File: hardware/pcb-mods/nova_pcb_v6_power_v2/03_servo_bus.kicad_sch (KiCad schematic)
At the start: 11 parts, among them J3 XT30_Inj, J4 XT30_Inj, J5 XT30_Inj, J6 XT30_Inj, J7 XT30_Inj, J8 ServoBus_TTL

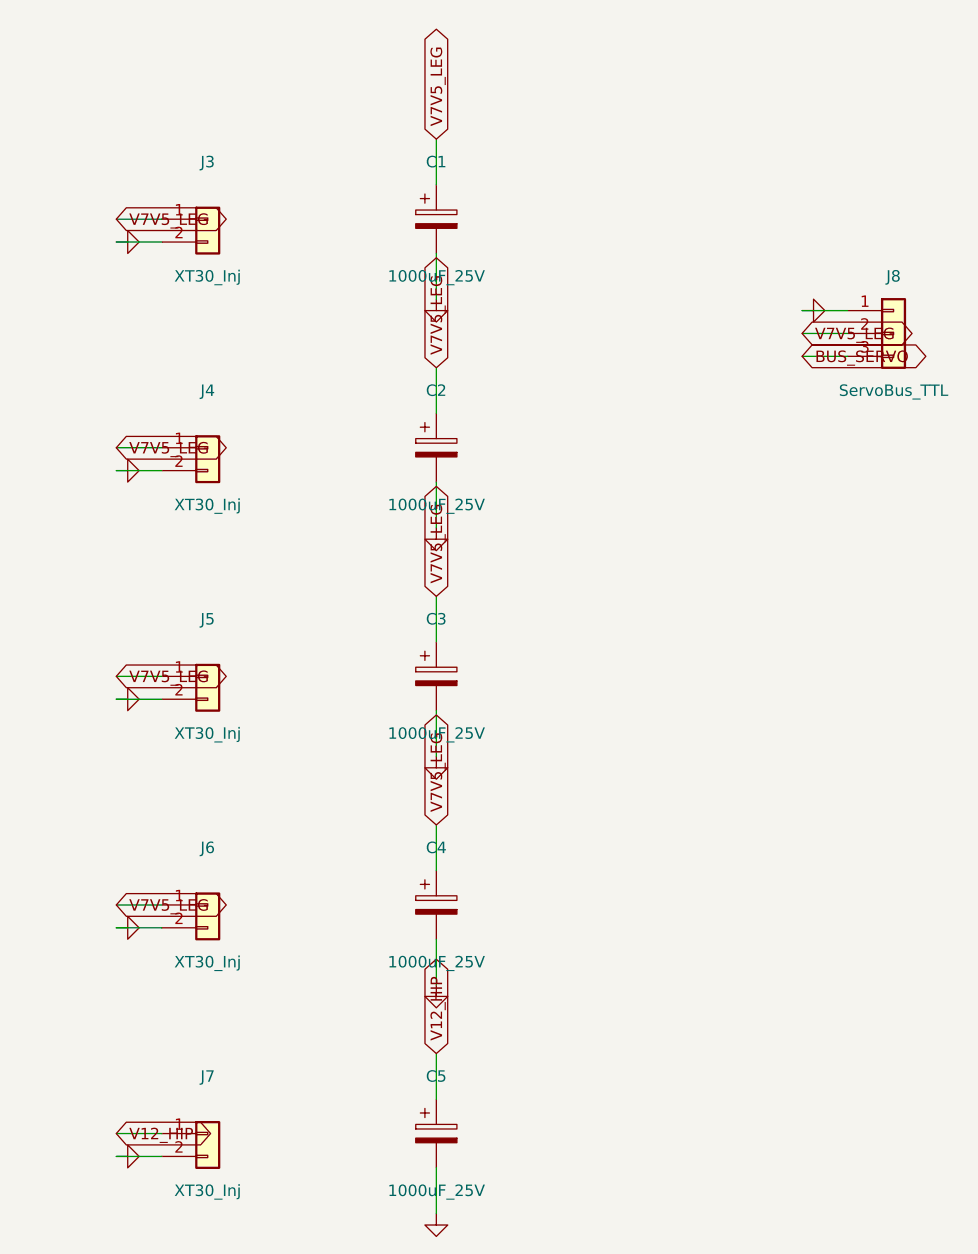
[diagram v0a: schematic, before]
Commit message: Chassis + leg_v6 CAD: no-drill assembly, leg fault audit (LA-1..28 + #47), fastener + gate hardening (#48)
* power board: arm Phase-4 routed + cleaned + fresh gerbers (fab-ready)

Completes the power board (blocker B1):
- U5.EN routed on EN_BUCKS (re-gate now realized on the board).
- V7V5_ARM 3mm, BATT_NEG/VBAT long runs 3mm, 21 high-current pads solid
  zone-connection (current-capacity fixes; TO-220/SW1 escapes left at 1.3mm).
- Removed the duplicate U12 + J14 (F8 UUID-mismatch artifacts) and the full
  orphan dangling-track chain they left behind.
- DRC: 0 hard, 0 unconnected, 0 dangling (10 cosmetic silk/lib only).
- Gerbers regenerated; fab_gate GO on both boards (J20 cross-board match OK).

DNP roster correct (U5 arm buck, U12 arm INA = Phase-4 reserve).

Co-Authored-By: Claude Opus 4.8 <noreply@anthropic.com>

* audit fixes 2026-06-18: NaN guard, pinout/battery/LVC doc sync, STATUS audit block

- main.cpp: NaN guard on commanded position (was UB (uint16_t)NaN -> 0 slam)
- teensy firmware/README.md: pinout table corrected to match main.cpp/PCB v6 (Serial1 0/1, E-stop 5, batt 4, active-LOW OE)
- power-budget.md + BOM.md: battery 4000->6000mAh (real Ovonic packs) + runtime/charge recompute
- BOM.md: bus driver order line -> SN74LVC125A (must be LVC, not 74HC125)
- STATUS.md: cross-domain audit section (open misalignments, weak points, questions)

Co-Authored-By: Claude Opus 4.8 <noreply@anthropic.com>

* docs: add servo-bus half-duplex timing bench checklist (pre-power-on §10)

Co-Authored-By: Claude Opus 4.8 <noreply@anthropic.com>

* docs: battery 4000->6000mAh sweep across secondary docs + STATUS CI-note fix

- 6000mAh 4S Ovonic (real pack) in cad-tooling, notes-qol (SoC math 5400mAh),
  order-list (bag), wiring diagram, README charger note, patterns pocket label
- dimensions.md + patterns.md: physical box/pocket dims flagged RE-MEASURE
  (6000mAh pack is larger; old 4000mAh dims kept as reference, not as truth)
- STATUS.md: corrected CI note (ros-pytest.yml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
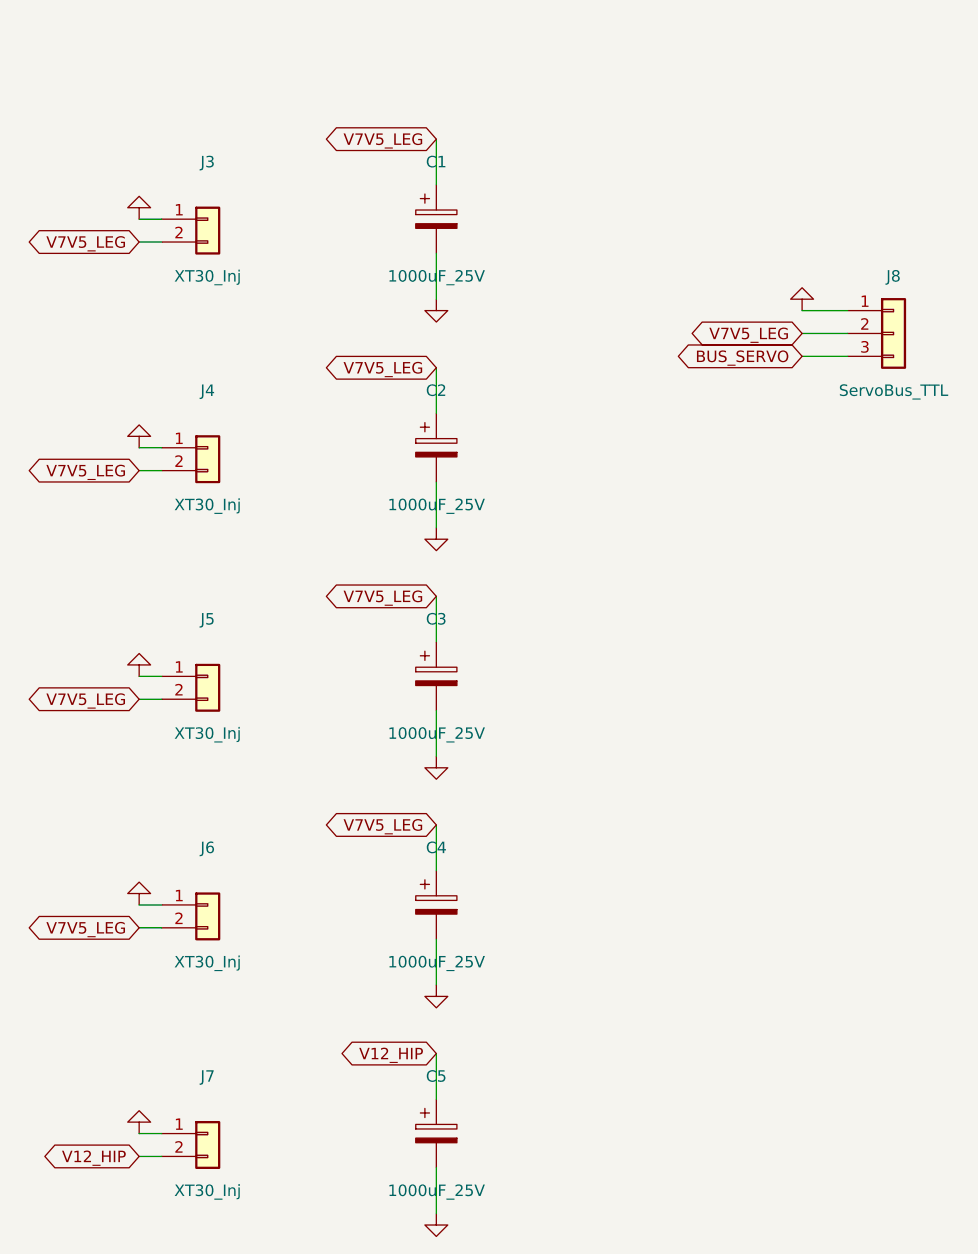
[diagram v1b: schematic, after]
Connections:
- net GND: now also J3.1 (Pin_1), J4.1 (Pin_1), J5.1 (Pin_1), J6.1 (Pin_1), J7.1 (Pin_1); no longer J3.2 (Pin_2), J4.2 (Pin_2), J5.2 (Pin_2), J6.2 (Pin_2), J7.2 (Pin_2)
- net V12_HIP: now also J7.2 (Pin_2); no longer J7.1 (Pin_1)
- net V7V5_LEG: now also J3.2 (Pin_2), J4.2 (Pin_2), J5.2 (Pin_2), J6.2 (Pin_2); no longer J3.1 (Pin_1), J4.1 (Pin_1), J5.1 (Pin_1), J6.1 (Pin_1)
